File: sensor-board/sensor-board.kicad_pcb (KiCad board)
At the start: 4 copper layers, 102 parts, among them J1 USB_C_Receptacle_USB2.0_16P, J10 cap4, J11 header pins, J2 aux pwr, J3 SWD, J4 water 1, J5 water 2, J6 relay, J7 cap1, J8 cap2, J9 cap3, K1 SIL03-1A72-71D, Q1 Si2312, Q2 Si2312, SW1 SW_Push, U1 MLPF-WB55-01E3, U10 EKMB130711, U11 DRV5032, U2 STM32WB55CCUx, U3 MCP1703Ax-300xxTT, U4 SHT40-AD1F-R2, U5 VL53L1CXV0FY1, U6 TLV4082, U7 CLS16D24-44, U8 LIS2DE12TR, U9 FDC2114RGHR, Y1 32.768KHz, Y2 32MHz

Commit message: Some board grouping, no traces yet
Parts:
- removed C14: 0.1uF, Capacitor_SMD:C_0402_1005Metric
- removed C7: 10nF, Capacitor_SMD:C_0402_1005Metric
- C2, C3: value 10pF -> 6.2pF
- moved J6 176.5 mm to (258.3, 31.9)
- moved J8 164.1 mm to (256.7, 97.8), turned to -90 degrees
- moved J7 163.9 mm to (256.7, 87.9), turned to -90 degrees
- moved J10 161.5 mm to (256.9, 117.6), turned to -90 degrees
- moved J9 161.2 mm to (256.9, 107.7), turned to -90 degrees
- moved U9 131.4 mm to (247.6, 103.1), turned to -90 degrees
- moved C24 131.3 mm to (244.6, 103.9), turned to -90 degrees
- moved Q1 131.3 mm to (40.2, 143.4), turned to 180 degrees
- moved R9 131.2 mm to (263.7, 45.0), turned to -90 degrees
- moved R12 130.3 mm to (262.1, 45.7), turned to 180 degrees
- moved C12 124.3 mm to (51.7, 142.5)
- moved C22 123.8 mm to (202.9, 152.4), turned to 90 degrees
- moved C15 123.6 mm to (51.7, 143.5)
- moved C19 123.5 mm to (204.0, 152.3), turned to 90 degrees
- moved R4 121.9 mm to (46.2, 146.8), turned to 90 degrees
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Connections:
- K1 pad 1: (no net) -> Net-(J6-Pin_1)
- K1 pad 3: (no net) -> +3V0
- K1 pad 5: (no net) -> Net-(D2-A)
- K1 pad 7: (no net) -> Net-(J6-Pin_2)
- Q1 pad 1: (no net) -> GND
- Q1 pad 2: (no net) -> Net-(BT1-+)
- Q1 pad 3: (no net) -> Net-(BT1--)

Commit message: Starting a little bit of routing; starting with HF crystal
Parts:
- removed C35: 1.0pF, Capacitor_SMD:C_0402_1005Metric
- removed L7: 3.9nH, Inductor_SMD:L_0402_1005Metric
- removed L8: 2.7nH, Inductor_SMD:L_0402_1005Metric
- added BT1: Battery_Cell, vendor:BatteryHolder_CR2032, F.Cu at (175.0, 132.2)
- AE1: value 2450AT18A100 -> Antenna; footprint vendor:XDCR_ACAG0801-2450-T -> vendor:Antenna_2.4GHz_InvertedF_SiLabs
- moved R4 140.8 mm to (173.5, 86.6), turned to 0 degrees
- moved JP2 140.0 mm to (175.4, 96.7), turned to 180 degrees
- moved Q1 139.1 mm to (172.7, 101.0), turned to -90 degrees
- moved R5 136.5 mm to (173.5, 89.7), turned to 0 degrees
- moved J1 135.7 mm to (167.7, 87.9), turned to -90 degrees
- moved U3 134.8 mm to (175.0, 91.4), turned to 90 degrees
- moved J3 134.0 mm to (170.9, 96.5), turned to 90 degrees
- moved C13 132.5 mm to (174.6, 93.8), turned to 180 degrees
- moved C11 131.8 mm to (174.6, 94.8), turned to 180 degrees
- moved R9 117.1 mm to (180.9, 127.8), turned to 180 degrees
- moved R12 115.0 mm to (180.1, 126.3), turned to 90 degrees
- moved Q2 114.9 mm to (182.5, 126.2), turned to -90 degrees
- moved U5 110.9 mm to (124.8, 77.6), turned to 90 degrees
- moved D2 109.6 mm to (183.1, 122.4), turned to -90 degrees
- moved C17 107.3 mm to (123.9, 80.9), turned to 180 degrees
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- renumbered C11 to C10, C12 to C11, C13 to C12, C15 to C13, C16 to C14, C17 to C15, C18 to C16, C19 to C17, C20 to C18, C21 to C19, C4 to C2, C22 to C20, C23 to C21, C24 to C22, C25 to C23, C26 to C24, C27 to C25, C28 to C26, C29 to C27, C30 to C28, C31 to C29, C2 to C3, C32 to C30, C33 to C31, C34 to C32, C5 to C4, C3 to C5, C8 to C7, C9 to C8, C10 to C9, J9 to J10, J10 to J11, J11 to J2, J2 to J3, J3 to J4, J4 to J5, J5 to J6, J6 to J7, J7 to J8, J8 to J9, TP6 to TP1, TP7 to TP2, TP8 to TP3, TP9 to TP4, TP10 to TP5, TP11 to TP6, TP12 to TP7, TP13 to TP8, Y2 to Y1, Y1 to Y2
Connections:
- net Net-(U1-IN) renamed /board rf
- net Net-(U2-OSC_IN) renamed /hf_osc+
- net Net-(U2-OSC_OUT) renamed /hf_osc-
- AE1 pad 1: Net-(AE1-A) -> /antenna-rf
- AE1 pad 2: (no net) -> GND
- U1 pad A1: Net-(U1-OUT) -> /antenna-rf
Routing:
- net /hf_osc-: track 0.00 -> 3.90 mm
- net /hf_osc+: track 0.00 -> 3.74 mm
- net GND: track 0.00 -> 3.34 mm, vias 0 -> 33
- net +3V0: track 0.00 -> 2.22 mm
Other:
- board outline added: 25.4 x 9.8 mm

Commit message: SMPS and (most of) LF crystal
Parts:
- moved C1 43.2 mm to (175.8, 60.0)
- moved L2 41.7 mm to (173.9, 60.4), turned to 90 degrees
- moved L1 40.1 mm to (175.8, 61.0), turned to 180 degrees
- moved C5 9.73 mm to (182.0, 49.6), turned to -90 degrees
- moved Y2 9.18 mm to (180.2, 50.6), turned to 90 degrees
- moved C6 7.49 mm to (177.2, 59.5)
- moved C3 6.96 mm to (182.0, 51.6), turned to 90 degrees
- moved C2 3.81 mm to (184.6, 54.3)
- moved C4 3.81 mm to (183.6, 54.3)
- moved C7 3.81 mm to (185.6, 54.3)
- moved C8 0.75 mm to (173.1, 49.5)
- moved R6 0.75 mm to (175.1, 49.4)
- moved R7 0.75 mm to (174.1, 49.4)
- moved C14 0.10 mm to (175.8, 59.1)
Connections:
- net Net-(U2-PC14) renamed /lf_osc+
- net Net-(U2-PC15) renamed /lf_osc-
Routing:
- net /lf_osc-: track 0.00 -> 6.81 mm
- net /lf_osc+: track 0.00 -> 6.58 mm
- net Net-(U2-VLXSMPS): track 0.00 -> 3.28 mm
- net GND: track 3.34 -> 6.61 mm, vias 33 -> 71
- net +3V0: track 2.22 -> 4.71 mm
- net Net-(U2-VFBSMPS): track 0.00 -> 1.75 mm
- net Net-(L1-Pad2): track 0.00 -> 1.53 mm

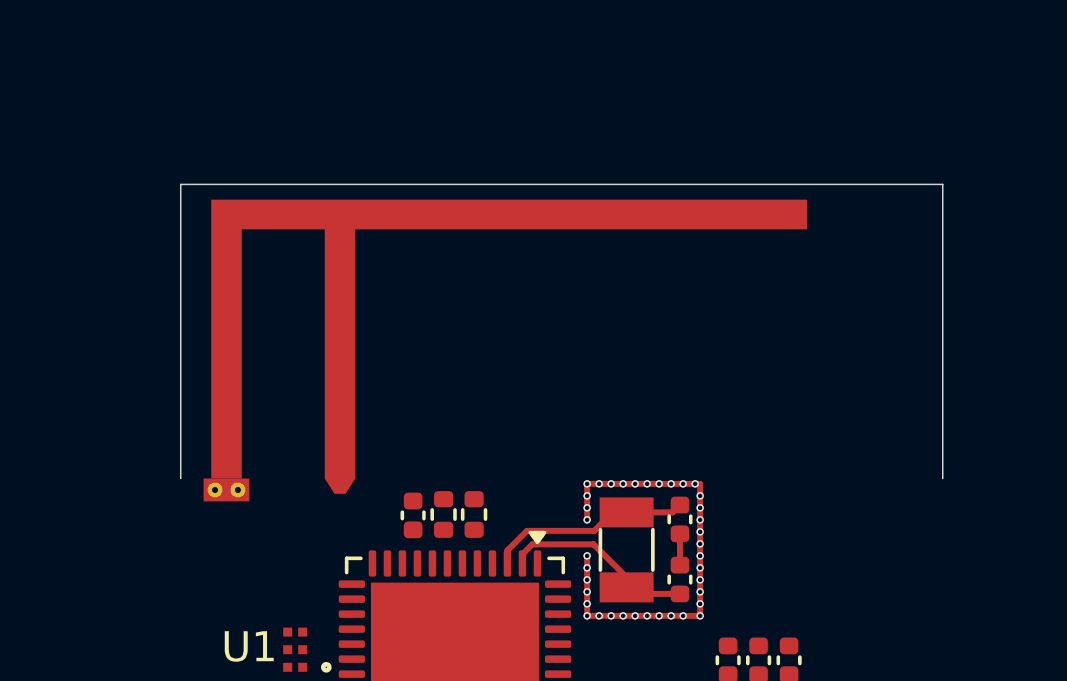
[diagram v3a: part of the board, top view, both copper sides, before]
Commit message: finish off LF crystal (except for GND connection)
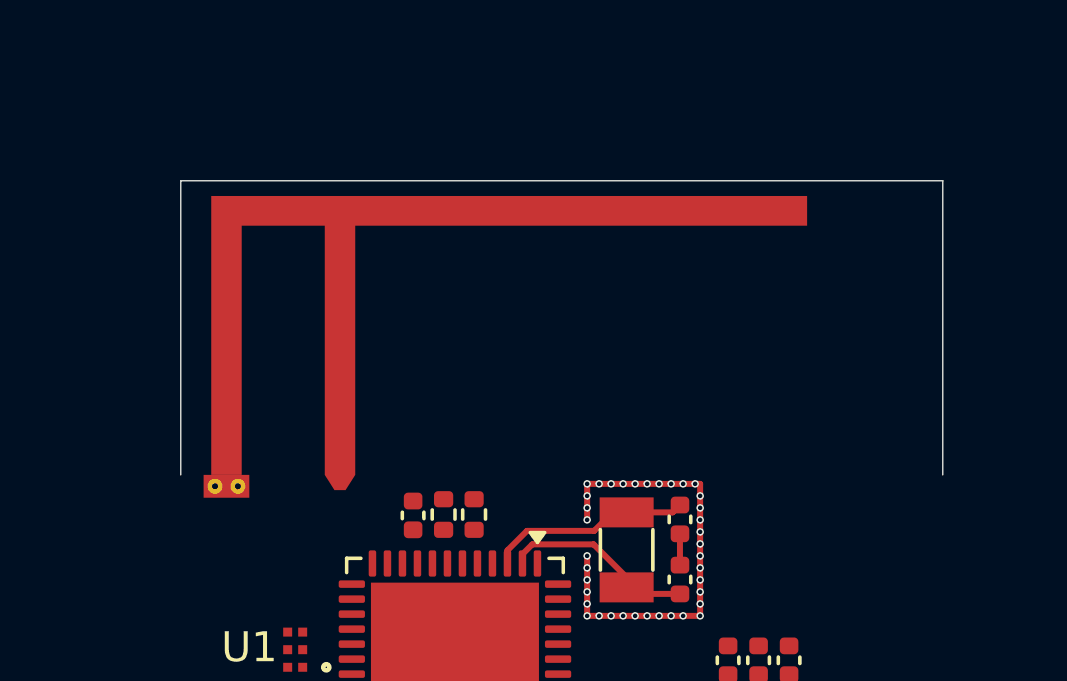
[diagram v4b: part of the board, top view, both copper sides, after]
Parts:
- moved AE1 0.12 mm to (166.4, 48.1)
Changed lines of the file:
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@@
 	(footprint "vendor:Antenna_2.4GHz_InvertedF_SiLabs"
 		(layer "F.Cu")
-		(at 166.37 48.2217)
+		(at 166.37 48.1)
 		(tags "antenna 2.4GHz")
 		(property "Reference" "AE1"
@@
 			(polygon
 				(pts
-					(xy 165.354 48.2217) (xy 165.354 38.4173) (xy 190.754 38.4173) (xy 190.754 48.2217)
+					(xy 165.354 48.1) (xy 165.354 38.2956) (xy 190.754 38.2956) (xy 190.754 48.1)
 				)
 			)
@@
 		(net "GND")
 	)
+	(gr_rect
+		(start 178.9 48.4)
+		(end 182.667 52.8)
+		(stroke
+			(width 0.2)
+			(type solid)
+		)
+		(fill yes)
+		(layer "In1.Cu")
+		(net "GND")
+	)
 	(segment
 		(start 176.23 57.943)
@@
 	)
 	(zone
+		(layers "F.Cu" "B.Cu" "In1.Cu" "In2.Cu")
+		(hatch edge 0.5)
+		(connect_pads
+			(clearance 0)
+		)
+		(min_thickness 0.25)
+		(keepout
+			(tracks allowed)
+			(vias allowed)
+			(pads allowed)
+			(copperpour not_allowed)
+			(footprints allowed)
+		)
+		(placement
+			(enabled no)
+			(sheetname "/")
+		)
+		(fill
+			(thermal_gap 0.5)
+			(thermal_bridge_width 0.5)
+			(island_removal_mode 0)
+		)
+		(polygon
+			(pts
+				(xy 178.6 48.1) (xy 178.6 53.1) (xy 182.95 53.1) (xy 182.95 48.1)
+			)
+		)
+	)
+	(zone

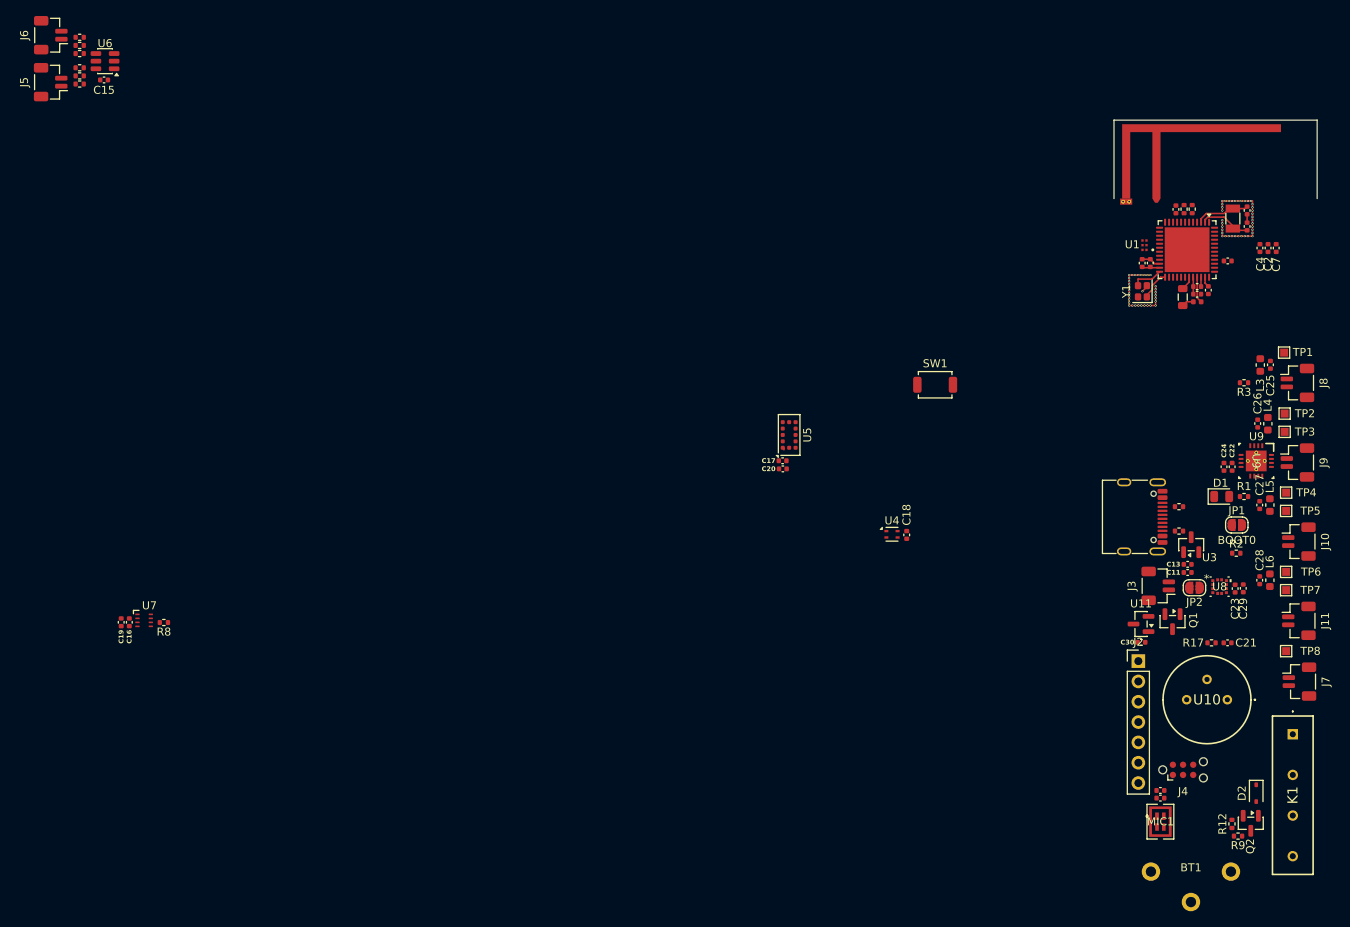
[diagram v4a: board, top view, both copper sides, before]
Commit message: ~Finished routing, not yet DRC-clean
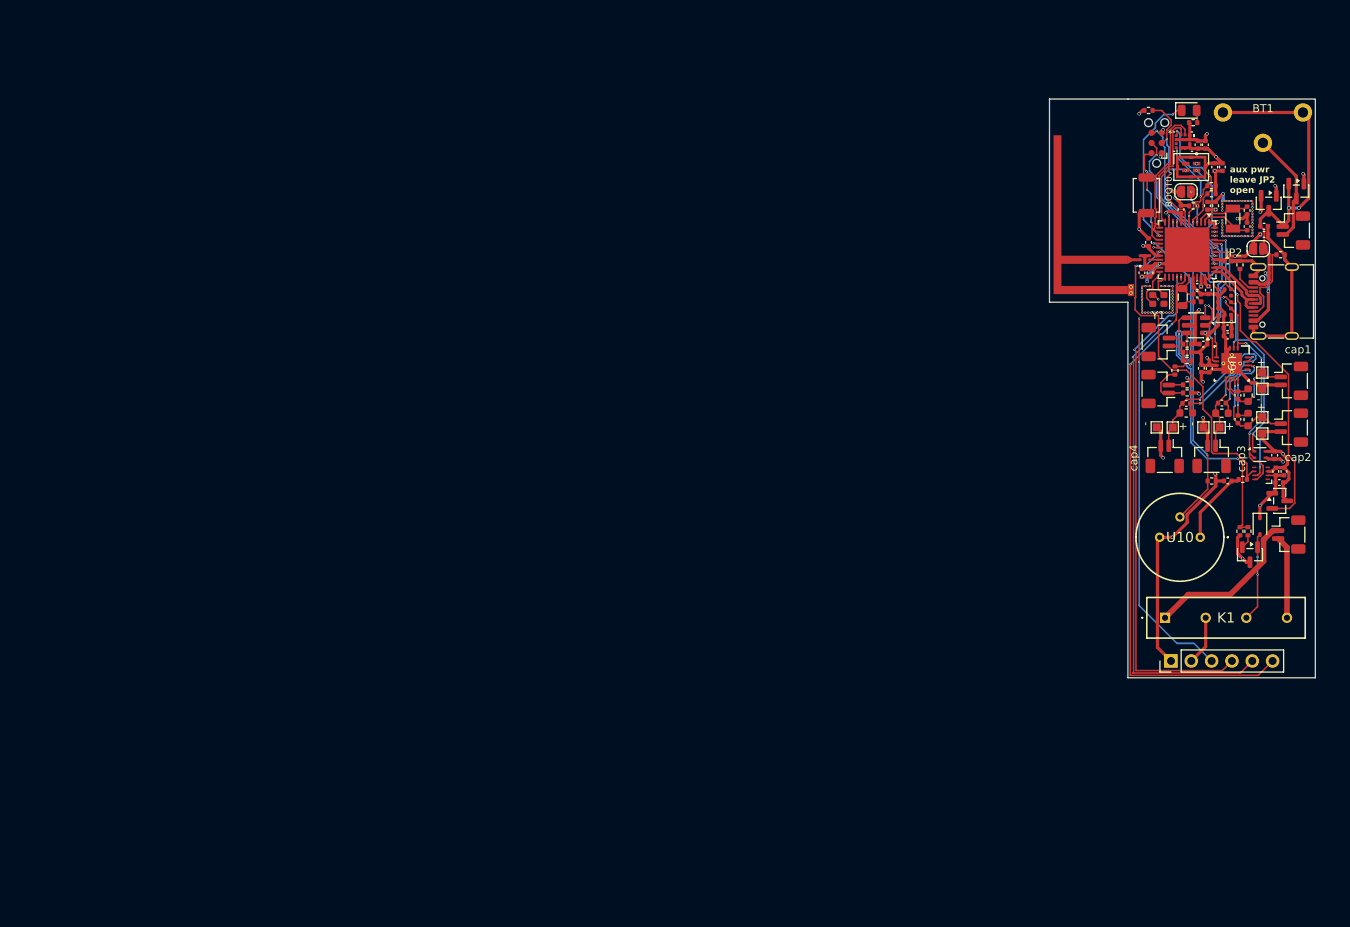
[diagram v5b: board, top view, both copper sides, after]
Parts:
- J2: value header pins -> Conn_01x06; footprint Connector_PinHeader_2.54mm:PinHeader_1x07_P2.54mm_Vertical -> Connector_PinHeader_2.54mm:PinHeader_1x06_P2.54mm_Vertical
- moved C19 146.6 mm to (186.6, 82.2), turned to 90 degrees
- moved C16 144.5 mm to (185.6, 82.2), turned to 90 degrees
- moved R13 144.0 mm to (174.5, 72.4)
- moved J5 143.6 mm to (170.9, 71.9)
- moved J6 143.6 mm to (170.9, 66.0)
- moved R11 143.6 mm to (174.5, 68.3)
- moved R14 143.6 mm to (174.5, 67.3)
- moved R16 143.6 mm to (174.5, 66.3)
- moved R15 143.4 mm to (174.5, 71.4)
- moved U7 142.3 mm to (184.6, 83.2), turned to 180 degrees
- moved R10 142.0 mm to (173.0, 69.6), turned to -90 degrees
- moved C15 141.3 mm to (176.5, 66.3)
- moved U6 140.3 mm to (175.6, 63.9)
- moved R8 136.0 mm to (181.5, 83.2), turned to 0 degrees
- moved BT1 95.3 mm to (184.0, 37.3)
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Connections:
- U2 pad 19: hp4 -> color_int
- U2 pad 30: hp5 -> hp4
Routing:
- net GND: track 6.61 -> 162.3 mm, vias 71 -> 90
- net +3V0: track 4.71 -> 89.8 mm, vias 0 -> 23
- net hp4: track 0.00 -> 71.5 mm, vias 0 -> 2
- net hp3: track 0.00 -> 67.7 mm, vias 0 -> 3
- net hp2: track 0.00 -> 64.4 mm, vias 0 -> 2
- net hp1: track 0.00 -> 58.6 mm, vias 0 -> 3
- net scl: track 0.00 -> 57.3 mm, vias 0 -> 6
- net sda: track 0.00 -> 55.9 mm, vias 0 -> 8
- net relay: track 0.00 -> 54.2 mm, vias 0 -> 2
- net Net-(BT1-+): track 0.00 -> 51.9 mm, vias 0 -> 4
- net motion: track 0.00 -> 42.1 mm, vias 0 -> 2
- net color_int: track 0.00 -> 42.0 mm, vias 0 -> 2
- net mag: track 0.00 -> 40.0 mm, vias 0 -> 2
- net Net-(J7-Pin_1): track 0.00 -> 20.2 mm
- net Net-(J11-Pin_1): track 0.00 -> 19.9 mm, vias 0 -> 2
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- added copper zone on In2.Cu, net +3V0
- added copper zone on In1.Cu, net GND
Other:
- board size 25.4 x 9.8 mm -> 23.4 x 72.3 mm
- board text added: "+"
- board text added: "-"
- board text added: "aux pwr leave JP2 open"
- board text added: "cap1"
- board text added: "cap2"
- board text added: "cap3"
- board text added: "cap4"

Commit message: Address some human-discovered issues
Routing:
- net color_int: track 42.0 -> 40.8 mm
- net GND: vias 90 -> 106
- added copper zone on B.Cu, net GND
- added copper zone on In2.Cu, net GND
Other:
- board text added: "CR nausicaa: as best you can (this might be a PITA), see if you can route SCL and SDA (for I²C) on the other side of a ground plane or power plane from any other parts/nets/pads/etc; got a lot of comms and they might interfere with stuff."

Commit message: DRC-clean
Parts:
- added R18: 2.2M, Resistor_SMD:R_0603_1608Metric, F.Cu at (188.9, 44.2)
- added R19: 1.0k, Resistor_SMD:R_0402_1005Metric, F.Cu at (189.4, 45.5)
- added R20: 1k, Resistor_SMD:R_0402_1005Metric, F.Cu at (178.2, 64.7)
- added R21: 1k, Resistor_SMD:R_0402_1005Metric, F.Cu at (177.2, 61.5)
- moved Q1 0.37 mm to (187.9, 46.9), turned to 90 degrees
- moved C23 0.09 mm to (175.9, 41.4)
- moved C29 0.09 mm to (176.9, 41.4)
- moved U8 0.09 mm to (174.1, 41.0)
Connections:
- Q1 pad 1: GND -> Net-(BT1--)
- Q1 pad 2: Net-(BT1-+) -> Net-(Q1-G)
- Q1 pad 3: Net-(BT1--) -> GND
- U6 pad 2: water1 -> Net-(U6-OUT1)
- U6 pad 3: water2 -> Net-(U6-OUT2)
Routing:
- net GND: track 162.3 -> 157.4 mm, vias 106 -> 86
- net +3V0: track 89.8 -> 85.8 mm, vias 23 -> 22
- net water2: track 13.5 -> 9.77 mm
- net water1: track 16.2 -> 12.5 mm, vias 2 -> 3
- net Net-(BT1-+): track 51.9 -> 49.4 mm
- net Net-(Q1-G): track 0.00 -> 2.34 mm
- net cap_int: track 16.7 -> 18.8 mm
- net Net-(U6-OUT1): track 0.00 -> 1.92 mm
- net cap_shut: track 16.8 -> 18.2 mm
- net hp1: track 58.6 -> 60.0 mm
- net sai1_d1: track 16.3 -> 15.0 mm
- net led: track 19.5 -> 20.8 mm
- net relay: track 54.2 -> 52.9 mm
- net Net-(U6-OUT2): track 0.00 -> 1.20 mm
- net motion: track 42.1 -> 41.0 mm
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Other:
- board text removed: "CR nausicaa: as best you can (this might be a PITA), see if you can route SCL and SDA (for I²C) on the other side of a ground plane or power plane from any other parts/nets/pads/etc; got a lot of comms and they might interfere with stuff."

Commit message: Fix all of claude's issues
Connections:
- Y1 pad 4: (no net) -> GND
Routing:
- net GND: track 157.4 -> 79.6 mm, vias 86 -> 193
- net relay: track 52.9 -> 43.4 mm
- net color_int: track 40.8 -> 37.8 mm
- net motion: track 41.0 -> 42.2 mm
- net +3V0: track 85.8 -> 84.6 mm
- net Net-(U9-IN3B): track 12.8 -> 11.8 mm
- net Net-(J10-Pin_1): track 13.1 -> 12.5 mm
- net Net-(J11-Pin_1): track 19.7 -> 19.2 mm
- added copper zone on F.Cu, net GND
